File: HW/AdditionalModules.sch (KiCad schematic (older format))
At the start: 23 parts, among them J40 ph_1x2, Q40 BC817, Q41 BC817, U40 AT_CryptoAuth, U41 HIH8000_I2C

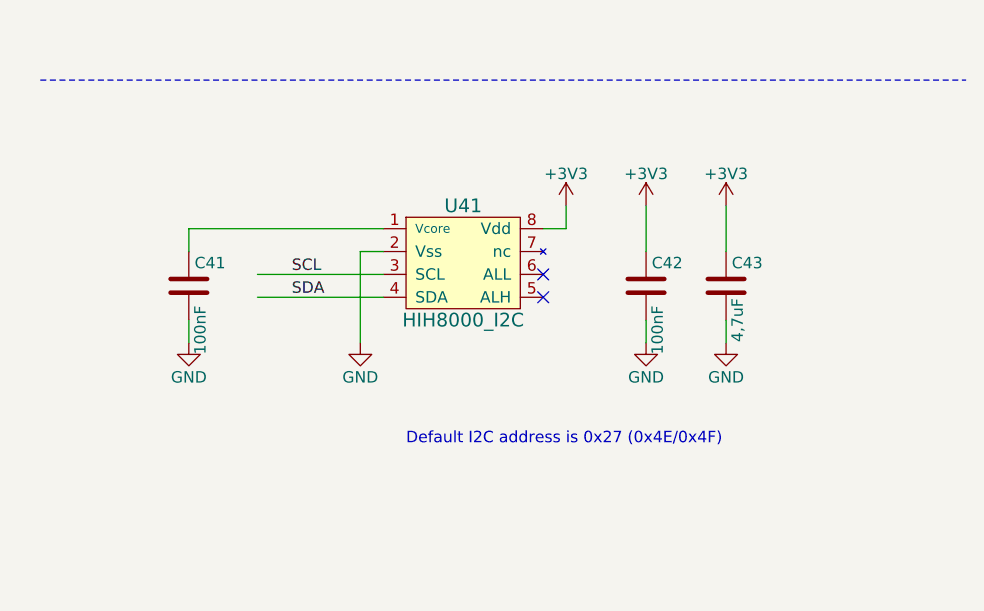
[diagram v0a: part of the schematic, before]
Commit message: Replaces the HIH8000 sensor with a HDC1080 sensor.
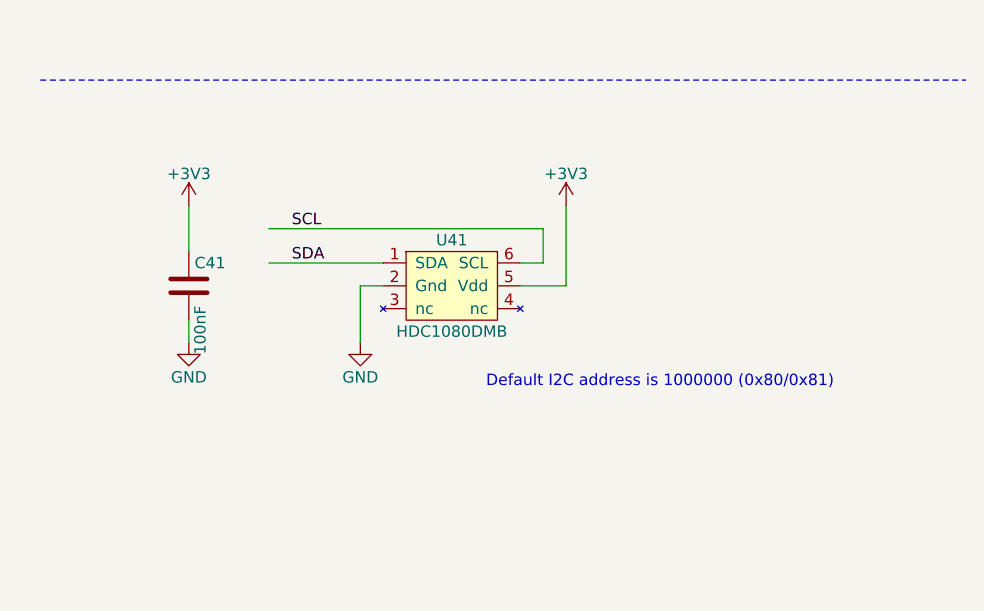
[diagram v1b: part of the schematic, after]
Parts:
- removed C42: 100nF, CalinGeneric:C0805HS, symbol calin:C
- removed C43: 4,7uF, CalinGeneric:C0805HS, symbol calin:C
- removed U41: HIH8000_I2C, CalinGeneric:SOIC-8-HS, symbol calin:HIH8000_I2C
- added U41: HDC1080DMB, CalinGeneric:WSON6-TI-HDC-HS, symbol calin:HDC1080DMB
- C41: Variant HIH -> Sensor
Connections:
- wire segments 55 -> 52
- no-connect marks 2 -> 0
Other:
- note added: "Default I2C address is 1000000 (0x80/0x81)"
- note removed: "Default I2C address is 0x27 (0x4E/0x4F)"
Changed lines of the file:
@@
 Sheet 3 3
 Title "ESP32 RFM69/RFM9x Gateway"
-Date "2019-05-02"
-Rev "35"
+Date "2019-05-03"
+Rev "36"
 Comp "Calin Radoni"
 Comment1 ""
@@
 	2750 7100 2750 7050
 $Comp
-L calin:HIH8000_I2C U41
-U 1 1 5CBE66CD
-P 8250 5400
-F 0 "U41" H 8250 5650 60  0000 C CNN
-F 1 "HIH8000_I2C" H 8250 5150 60  0000 C CNN
-F 2 "CalinGeneric:SOIC-8-HS" H 8250 5400 60  0001 C CNN
-F 3 "" H 8250 5400 60  0000 C CNN
-F 4 "HIH" H 550 0   50  0001 C CNN "Variant"
-F 5 "HIH8130-021-001 / HIH8131-021-001" H 550 0   50  0001 C CNN "part-number"
-F 6 "+/- 2.0 RH Accuracy" H 550 0   50  0001 C CNN "characteristics"
-F 7 "Honeywell" H 550 0   50  0001 C CNN "manufacturer"
-F 8 "SOIC-8 3.90mm" H 550 0   50  0001 C CNN "package"
-	1    8250 5400
-	1    0    0    -1
-$EndComp
-$Comp
 L power:GND #PWR?
 U 1 1 5CBEDDD9
@@
 	1    0    0    -1
 $EndComp
-Wire Wire Line
-	8700 5150 8700 5250
-Wire Wire Line
-	8700 5250 8600 5250
-Wire Wire Line
-	7900 5350 7800 5350
-Wire Wire Line
-	7800 5350 7800 5750
 $Comp
 L calin:C C?
@@
 F 2 "CalinGeneric:C0805HS" H 7088 5350 50  0001 C CNN
 F 3 "" H 7050 5500 50  0000 C CNN
-F 4 "HIH" H 550 0   50  0001 C CNN "Variant"
+F 4 "Sensor" H 550 0   50  0001 C CNN "Variant"
 F 5 "100 nF / 50V / X7R" H 550 0   50  0001 C CNN "characteristics"
 F 6 "Samsung" H 550 0   50  0001 C CNN "manufacturer"
@@
 	1    0    0    -1
 $EndComp
-$Comp
-L calin:C C?
-U 1 1 5CBF00B7
-P 9050 5500
-AR Path="/5CBF00B7" Ref="C?"  Part="1"
-AR Path="/5CCB086C/5CBF00B7" Ref="C42"  Part="1"
-F 0 "C42" H 9075 5600 50  0000 L CNN
-F 1 "100nF" V 9100 5200 50  0000 L CNN
-F 2 "CalinGeneric:C0805HS" H 9088 5350 50  0001 C CNN
-F 3 "" H 9050 5500 50  0000 C CNN
-F 4 "HIH" H 650 0   50  0001 C CNN "Variant"
-F 5 "100 nF / 50V / X7R" H 650 0   50  0001 C CNN "characteristics"
-F 6 "Samsung" H 650 0   50  0001 C CNN "manufacturer"
-F 7 "0805" H 650 0   50  0001 C CNN "package"
-F 8 "CL21B104KBCNNNC" H 650 0   50  0001 C CNN "part-number"
-	1    9050 5500
-	1    0    0    -1
-$EndComp
-Wire Wire Line
-	7900 5450 7350 5450
-Wire Wire Line
-	7900 5550 7350 5550
-Text Label 7500 5550 0    50   ~ 0
+Text Label 7500 5400 0    50   ~ 0
 SDA
-Text Label 7500 5450 0    50   ~ 0
+Text Label 7500 5250 0    50   ~ 0
 SCL
 $Comp
@@
 L power:+3V3 #PWR?
 U 1 1 5CBF4B8D
-P 9050 5150
+P 7050 5150
 AR Path="/5CBF4B8D" Ref="#PWR?"  Part="1"
 AR Path="/5CCB086C/5CBF4B8D" Ref="#PWR0174"  Part="1"
-F 0 "#PWR0174" H 9050 5000 50  0001 C CNN
-F 1 "+3V3" H 9050 5290 50  0000 C CNN
-F 2 "" H 9050 5150 50  0000 C CNN
-F 3 "" H 9050 5150 50  0000 C CNN
-	1    9050 5150
-	1    0    0    -1
-$EndComp
-$Comp
-L power:GND #PWR?
-U 1 1 5CBF4BC0
-P 9050 5750
-AR Path="/5CBF4BC0" Ref="#PWR?"  Part="1"
-AR Path="/5CCB086C/5CBF4BC0" Ref="#PWR0175"  Part="1"
-F 0 "#PWR0175" H 9050 5500 50  0001 C CNN
-F 1 "GND" H 9050 5600 50  0000 C CNN
-F 2 "" H 9050 5750 50  0000 C CNN
-F 3 "" H 9050 5750 50  0000 C CNN
-	1    9050 5750
-	1    0    0    -1
-$EndComp
-Wire Wire Line
-	9050 5750 9050 5650
-Wire Wire Line
-	9050 5350 9050 5150
-NoConn ~ 8600 5450
-NoConn ~ 8600 5550
-Wire Wire Line
-	7900 5250 7050 5250
-Wire Wire Line
-	7050 5250 7050 5350
-$Comp
-L calin:C C?
-U 1 1 5CC12D9F
-P 9400 5500
-AR Path="/5CC12D9F" Ref="C?"  Part="1"
-AR Path="/5CCB086C/5CC12D9F" Ref="C43"  Part="1"
-F 0 "C43" H 9425 5600 50  0000 L CNN
-F 1 "4,7uF" V 9450 5350 50  0000 C CNN
-F 2 "CalinGeneric:C0805HS" H 9438 5350 50  0001 C CNN
-F 3 "" H 9400 5500 50  0000 C CNN
-F 4 "4.7 µF / 16 V / X7R" H 3250 3850 50  0001 C CNN "characteristics"
-F 5 "AVX" H 3250 3850 50  0001 C CNN "manufacturer"
-F 6 "0805" H 3250 3850 50  0001 C CNN "package"
-F 7 "0805YC475KAT2A" H 3250 3850 50  0001 C CNN "part-number"
-	1    9400 5500
-	1    0    0    -1
-$EndComp
-$Comp
-L power:+3V3 #PWR?
-U 1 1 5CC12DA5
-P 9400 5150
-AR Path="/5CC12DA5" Ref="#PWR?"  Part="1"
-AR Path="/5CCB086C/5CC12DA5" Ref="#PWR0176"  Part="1"
-F 0 "#PWR0176" H 9400 5000 50  0001 C CNN
-F 1 "+3V3" H 9400 5290 50  0000 C CNN
-F 2 "" H 9400 5150 50  0000 C CNN
-F 3 "" H 9400 5150 50  0000 C CNN
-	1    9400 5150
-	1    0    0    -1
-$EndComp
-$Comp
-L power:GND #PWR?
-U 1 1 5CC12DAB
-P 9400 5750
-AR Path="/5CC12DAB" Ref="#PWR?"  Part="1"
-AR Path="/5CCB086C/5CC12DAB" Ref="#PWR0177"  Part="1"
-F 0 "#PWR0177" H 9400 5500 50  0001 C CNN
-F 1 "GND" H 9400 5600 50  0000 C CNN
-F 2 "" H 9400 5750 50  0000 C CNN
-F 3 "" H 9400 5750 50  0000 C CNN
-	1    9400 5750
-	1    0    0    -1
-$EndComp
-Wire Wire Line
-	9400 5150 9400 5350
-Wire Wire Line
-	9400 5650 9400 5750
+F 0 "#PWR0174" H 7050 5000 50  0001 C CNN
+F 1 "+3V3" H 7050 5290 50  0000 C CNN
+F 2 "" H 7050 5150 50  0000 C CNN
+F 3 "" H 7050 5150 50  0000 C CNN
+	1    7050 5150
+	1    0    0    -1
+$EndComp
 Text Notes 2200 4950 0    50   ~ 0
 Default I2C Address of:\n- ATSHA204A is 0xC8/0xC9\n- ATECC508A is 0xC0/0xC1\n- ATECC608A is 0xC4/0xC5 (probably)
-Text Notes 8000 6200 0    50   ~ 0
-Default I2C address is 0x27 (0x4E/0x4F)
+Text Notes 8350 5950 0    50   ~ 0
+Default I2C address is 1000000 (0x80/0x81)
 Wire Notes Line width 20 style dotted
 	5650 1100 5650 7100
@@
 Wire Wire Line
 	7700 1300 7200 1300
+$Comp
+L calin:HDC1080DMB U41
+U 1 1 5CCCFB95
+P 8200 5500
+F 0 "U41" H 8200 5700 50  0000 C CNN
+F 1 "HDC1080DMB" H 8200 5300 50  0000 C CNN
+F 2 "CalinGeneric:WSON6-TI-HDC-HS" H 8200 5500 50  0001 C CNN
+F 3 "" H 8200 5500 50  0001 C CNN
+F 4 "Texas Instruments" H 8200 5800 50  0001 C CNN "manufacturer"
+F 5 "HDC1080DMB" H 8200 5850 50  0001 C CNN "part-number"
+F 6 "I2C Humidity and Temperature Sensor" H 8200 5900 50  0001 C CNN "characteristics"
+F 7 "WSON6" H 8200 5950 50  0001 C CNN "package"
+F 8 "Sensor" H 0   0   50  0001 C CNN "Variant"
+	1    8200 5500
+	1    0    0    -1
+$EndComp
+Wire Wire Line
+	7050 5150 7050 5350
+Wire Wire Line
+	7900 5500 7800 5500
+Wire Wire Line
+	7800 5500 7800 5750
+Wire Wire Line
+	8700 5150 8700 5500
+Wire Wire Line
+	8700 5500 8500 5500
+Wire Wire Line
+	7900 5400 7400 5400
+Wire Wire Line
+	8500 5400 8600 5400
+Wire Wire Line
+	8600 5400 8600 5250
+Wire Wire Line
+	8600 5250 7400 5250
 $EndSCHEMATC

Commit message: Adds a capacitor for humidity sensor, extended I2C socket or LEDs.
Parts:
- added C10: 10uF, CalinGeneric:C0805HS, symbol calin:C
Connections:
- wire segments 52 -> 54
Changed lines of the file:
@@
 Sheet 3 3
 Title "ESP32 RFM69/RFM9x Gateway"
-Date "2019-05-04"
-Rev "37"
+Date "2019-05-06"
+Rev "38"
 Comp "Calin Radoni"
 Comment1 ""
@@
 Wire Wire Line
 	8600 5250 7400 5250
+$Comp
+L calin:C C?
+U 1 1 5CD1A826
+P 8200 3850
+AR Path="/5CD1A826" Ref="C?"  Part="1"
+AR Path="/5CCB086C/5CD1A826" Ref="C10"  Part="1"
+F 0 "C10" H 8225 3950 50  0000 L CNN
+F 1 "10uF" V 8250 3550 50  0000 L CNN
+F 2 "CalinGeneric:C0805HS" H 8238 3700 50  0001 C CNN
+F 3 "" H 8200 3850 50  0000 C CNN
+F 4 "test" H 1700 -1650 50  0001 C CNN "Variant"
+F 5 "10 µF / 6,3 V" H 1700 -1650 50  0001 C CNN "characteristics"
+F 6 "Samsung" H 1700 -1650 50  0001 C CNN "manufacturer"
+F 7 "0805" H 1700 -1650 50  0001 C CNN "package"
+F 8 "CL21B106KQQNNNE" H 1700 -1650 50  0001 C CNN "part-number"
+	1    8200 3850
+	1    0    0    -1
+$EndComp
+$Comp
+L power:GND #PWR?
+U 1 1 5CD1A82C
+P 8200 4100
+AR Path="/5CD1A82C" Ref="#PWR?"  Part="1"
+AR Path="/5CCB086C/5CD1A82C" Ref="#PWR?"  Part="1"
+F 0 "#PWR?" H 8200 3850 50  0001 C CNN
+F 1 "GND" H 8200 3950 50  0000 C CNN
+F 2 "" H 8200 4100 50  0000 C CNN
+F 3 "" H 8200 4100 50  0000 C CNN
+	1    8200 4100
+	1    0    0    -1
+$EndComp
+Wire Wire Line
+	8200 4000 8200 4100
+$Comp
+L power:+3V3 #PWR?
+U 1 1 5CD1A833
+P 8200 3600
+AR Path="/5CD1A833" Ref="#PWR?"  Part="1"
+AR Path="/5CCB086C/5CD1A833" Ref="#PWR?"  Part="1"
+F 0 "#PWR?" H 8200 3450 50  0001 C CNN
+F 1 "+3V3" H 8200 3740 50  0000 C CNN
+F 2 "" H 8200 3600 50  0000 C CNN
+F 3 "" H 8200 3600 50  0000 C CNN
+	1    8200 3600
+	1    0    0    -1
+$EndComp
+Wire Wire Line
+	8200 3600 8200 3700
 $EndSCHEMATC

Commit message: Updates some part numbers.
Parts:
- C10: Variant test -> (none)
- C40, U40: Notes (none) -> DNP
- Q40, Q41: part-number BC817-40Q -> BC817-40
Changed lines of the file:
@@
 Sheet 3 3
 Title "ESP32 RFM69/RFM9x Gateway"
-Date "2019-05-06"
+Date "2019-05-18"
 Rev "38"
 Comp "Calin Radoni"
@@
 F 7 "Microchip" H 0   -200 50  0001 C CNN "manufacturer"
 F 8 "SOIC-8 3.90mm" H 0   -200 50  0001 C CNN "package"
+F 9 "DNP" H 0   0   50  0001 C CNN "Notes"
 	1    2200 4250
 	1    0    0    -1
@@
 F 7 "0805" H 0   -200 50  0001 C CNN "package"
 F 8 "CL21B104KBCNNNC" H 0   -200 50  0001 C CNN "part-number"
+F 9 "DNP" H 0   0   50  0001 C CNN "Notes"
 	1    1350 4250
 	1    0    0    -1
@@
 F 5 "Diodes" H 0   0   50  0001 C CNN "manufacturer"
 F 6 "SOT-23" H 0   0   50  0001 C CNN "package"
-F 7 "BC817-40Q" H 0   0   50  0001 C CNN "part-number"
+F 7 "BC817-40" H 0   0   50  0001 C CNN "part-number"
 	1    2650 6250
 	1    0    0    -1
@@
 F 5 "Diodes" H 0   0   50  0001 C CNN "manufacturer"
 F 6 "SOT-23" H 0   0   50  0001 C CNN "package"
-F 7 "BC817-40Q" H 0   0   50  0001 C CNN "part-number"
+F 7 "BC817-40" H 0   0   50  0001 C CNN "part-number"
 	1    2650 6850
 	1    0    0    1
@@
 F 2 "CalinGeneric:C0805HS" H 8238 3700 50  0001 C CNN
 F 3 "" H 8200 3850 50  0000 C CNN
-F 4 "test" H 1700 -1650 50  0001 C CNN "Variant"
-F 5 "10 µF / 6,3 V" H 1700 -1650 50  0001 C CNN "characteristics"
-F 6 "Samsung" H 1700 -1650 50  0001 C CNN "manufacturer"
-F 7 "0805" H 1700 -1650 50  0001 C CNN "package"
-F 8 "CL21B106KQQNNNE" H 1700 -1650 50  0001 C CNN "part-number"
+F 4 "10 µF / 6,3 V" H 1700 -1650 50  0001 C CNN "characteristics"
+F 5 "Samsung" H 1700 -1650 50  0001 C CNN "manufacturer"
+F 6 "0805" H 1700 -1650 50  0001 C CNN "package"
+F 7 "CL21B106KQQNNNE" H 1700 -1650 50  0001 C CNN "part-number"
 	1    8200 3850
 	1    0    0    -1

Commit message: Adds Antenna and Enclosure as components for schematic and BOM.
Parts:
- added SYM6: Antenna 868MHz, CalinGeneric:VirtualFootprint, symbol calin:Symbol_Antenna
- added SYM9: Enclosure, CalinGeneric:VirtualFootprint, symbol calin:Symbol_Enclosure
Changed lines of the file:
@@
 P 8200 4100
 AR Path="/5CD1A82C" Ref="#PWR?"  Part="1"
-AR Path="/5CCB086C/5CD1A82C" Ref="#PWR?"  Part="1"
-F 0 "#PWR?" H 8200 3850 50  0001 C CNN
+AR Path="/5CCB086C/5CD1A82C" Ref="#PWR0169"  Part="1"
+F 0 "#PWR0169" H 8200 3850 50  0001 C CNN
 F 1 "GND" H 8200 3950 50  0000 C CNN
 F 2 "" H 8200 4100 50  0000 C CNN
@@
 P 8200 3600
 AR Path="/5CD1A833" Ref="#PWR?"  Part="1"
-AR Path="/5CCB086C/5CD1A833" Ref="#PWR?"  Part="1"
-F 0 "#PWR?" H 8200 3450 50  0001 C CNN
+AR Path="/5CCB086C/5CD1A833" Ref="#PWR0170"  Part="1"
+F 0 "#PWR0170" H 8200 3450 50  0001 C CNN
 F 1 "+3V3" H 8200 3740 50  0000 C CNN
 F 2 "" H 8200 3600 50  0000 C CNN
@@
 Wire Wire Line
 	8200 3600 8200 3700
+$Comp
+L calin:Symbol_Enclosure SYM9
+U 1 1 5CE0FF1C
+P 3800 2650
+F 0 "SYM9" H 4050 2650 50  0001 C CNN
+F 1 "Enclosure" H 3978 2675 50  0000 L CNN
+F 2 "CalinGeneric:VirtualFootprint" H 3800 2650 50  0001 C CNN
+F 3 "" H 3800 2650 50  0001 C CNN
+F 4 "Gainta G706 (dark grey) or G738 (light grey)" H 800 50  50  0001 C CNN "characteristics"
+F 5 "Gainta" H 0   0   50  0001 C CNN "manufacturer"
+F 6 "*" H 0   0   50  0001 C CNN "package"
+F 7 "Gainta G706" H 0   0   50  0001 C CNN "part-number"
+	1    3800 2650
+	1    0    0    -1
+$EndComp
+$Comp
+L calin:Symbol_Antenna SYM6
+U 1 1 5CE1322C
+P 3900 2200
+F 0 "SYM6" H 4050 2250 50  0001 C CNN
+F 1 "Antenna 868MHz" H 3950 2200 50  0000 L CNN
+F 2 "CalinGeneric:VirtualFootprint" H 3900 2200 50  0001 C CNN
+F 3 "" H 3900 2200 50  0001 C CNN
+F 4 "868 MHz, 90 deg. SMA Male connector" H 0   -150 50  0001 C CNN "characteristics"
+F 5 "SR Passives" H 0   -150 50  0001 C CNN "manufacturer"
+F 6 "*" H 0   -150 50  0001 C CNN "package"
+F 7 "868M-ANT410" H 0   -150 50  0001 C CNN "part-number"
+	1    3900 2200
+	1    0    0    -1
+$EndComp
 $EndSCHEMATC
